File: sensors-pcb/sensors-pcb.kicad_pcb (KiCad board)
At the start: 2 copper layers, 75 x 55 mm, 60 parts, among them J1 Network Connector, J2 STDC14, J3 Conn_Coaxial, SW1 SW_Push, U1 MAX-M8Q, U3 LD39050PU33R, U4 STM32G474RBT6, U5 SN65HVD230, U6 MPU-6050, Y2 8MHz

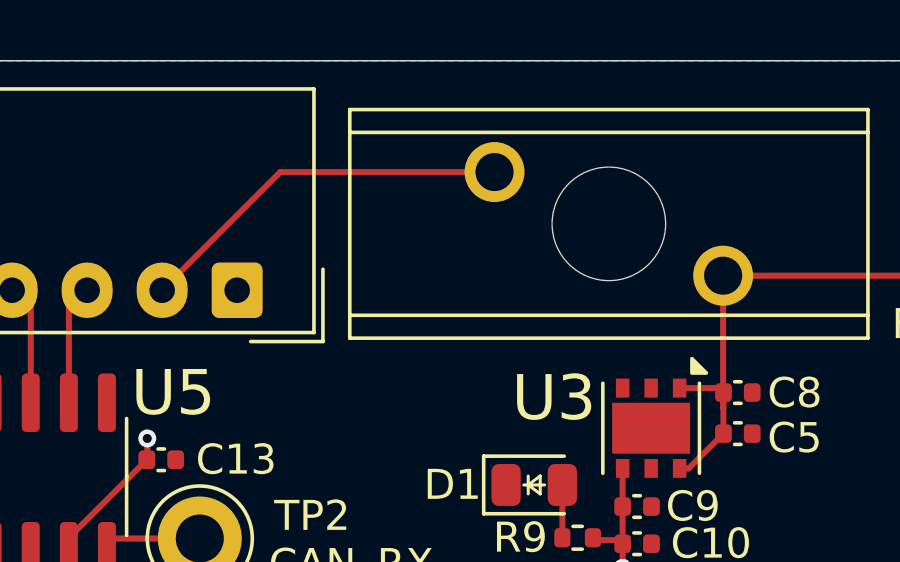
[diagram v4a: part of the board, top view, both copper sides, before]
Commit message: sensors-pcb: add test point for fuse
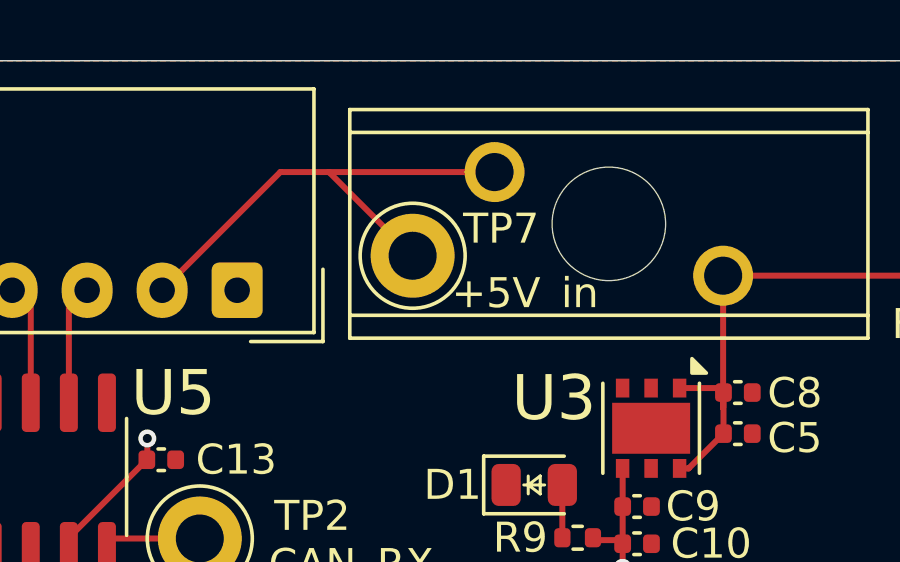
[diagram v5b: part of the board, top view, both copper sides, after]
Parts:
- added TP7: TestPoint, TestPoint:TestPoint_Keystone_5005-5009_Compact, F.Cu at (227.8, 28.0)
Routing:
- net Net-(J1-+5V): track 12.7 -> 16.7 mm
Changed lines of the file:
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@@
 		)
 	)
+	(footprint "TestPoint:TestPoint_Keystone_5005-5009_Compact"
+		(layer "F.Cu")
+		(at 227.85 28)
+		(descr "Keystone THM Compact Test Point 5005-5009, http://www.keyelco.com/product-pdf.cfm?p=1314")
+		(tags "Through Hole Mount Test Points")
+		(property "Reference" "TP7"
+			(at 2.95 -0.9 0)
+			(layer "F.SilkS")
+			(effects
+				(font
+					(size 1 1)
+					(thickness 0.15)
+				)
+			)
+		)
+		(property "Value" "TestPoint"
+			(at 0 3.15 0)
+			(layer "F.Fab")
+			(hide yes)
+			(effects
+				(font
+					(size 1 1)
+					(thickness 0.15)
+				)
+			)
+		)
+		(property "Datasheet" "https://www.keyelco.com/userAssets/file/M65p56.pdf"
+			(at 0 0 0)
+			(unlocked yes)
+			(layer "F.Fab")
+			(hide yes)
+			(effects
+				(font
+					(size 1.27 1.27)
+					(thickness 0.15)
+				)
+			)
+		)
+		(property "Description" "test point"
+			(at 0 0 0)
+			(unlocked yes)
+			(layer "F.Fab")
+			(hide yes)
+			(effects
+				(font
+					(size 1.27 1.27)
+					(thickness 0.15)
+				)
+			)
+		)
+		(property "Net Label" "+5V_in"
+			(at 3.75 1.25 0)
+			(unlocked yes)
+			(layer "F.SilkS")
+			(effects
+				(font
+					(size 1 1)
+					(thickness 0.15)
+				)
+			)
+		)
+		(property ki_fp_filters "Pin* Test*")
+		(sheetname "/STM32 Base Layout/")
+		(sheetfile "stm32_base.kicad_sch")
+		(attr through_hole dnp)
+		(fp_circle
+			(center 0 0)
+			(end 1.75 0)
+			(stroke
+				(width 0.12)
+				(type solid)
+			)
+			(fill no)
+			(layer "F.SilkS")
+		)
+		(fp_circle
+			(center 0 0)
+			(end 2 0)
+			(stroke
+				(width 0.05)
+				(type solid)
+			)
+			(fill no)
+			(layer "F.CrtYd")
+		)
+		(fp_rect
+			(start -1.25 -0.4)
+			(end 1.25 0.4)
+			(stroke
+				(width 0.1)
+				(type default)
+			)
+			(fill no)
+			(layer "F.Fab")
+		)
+		(fp_circle
+			(center 0 0)
+			(end 1.6 0)
+			(stroke
+				(width 0.1)
+				(type solid)
+			)
+			(fill no)
+			(layer "F.Fab")
+		)
+		(fp_text user "${REFERENCE}"
+			(at 0 0 0)
+			(layer "F.Fab")
+			(effects
+				(font
+					(size 0.6 0.6)
+					(thickness 0.09)
+				)
+			)
+		)
+		(pad "1" thru_hole circle
+			(at 0 0)
+			(size 2.8 2.8)
+			(drill 1.6)
+			(layers "*.Cu" "*.Mask")
+			(remove_unused_layers no)
+			(net 9 "Net-(J1-+5V)")
+			(pinfunction "1")
+			(pintype "passive")
+		)
+		(embedded_fonts no)
+		(model "${KICAD9_3DMODEL_DIR}/TestPoint.3dshapes/TestPoint_Keystone_5005-5009_Compact.step"
+			(offset
+				(xyz 0 0 0)
+			)
+			(scale
+				(xyz 1 1 1)
+			)
+			(rotate
+				(xyz 0 0 0)
+			)
+		)
+	)
 	(footprint "Exocet:Fuse_Holder_Littelfuse_01530008"
 		(layer "F.Cu")
@@
 	(segment
 		(start 223.44 25.21)
+		(end 225.06 25.21)
+		(width 0.2)
+		(layer "F.Cu")
+		(net 9)
+	)
+	(segment
+		(start 227.85 28)
+		(end 225.06 25.21)
+		(width 0.2)
+		(layer "F.Cu")
+		(net 9)
+	)
+	(segment
+		(start 225.06 25.21)
 		(end 230.58 25.21)
 		(width 0.2)

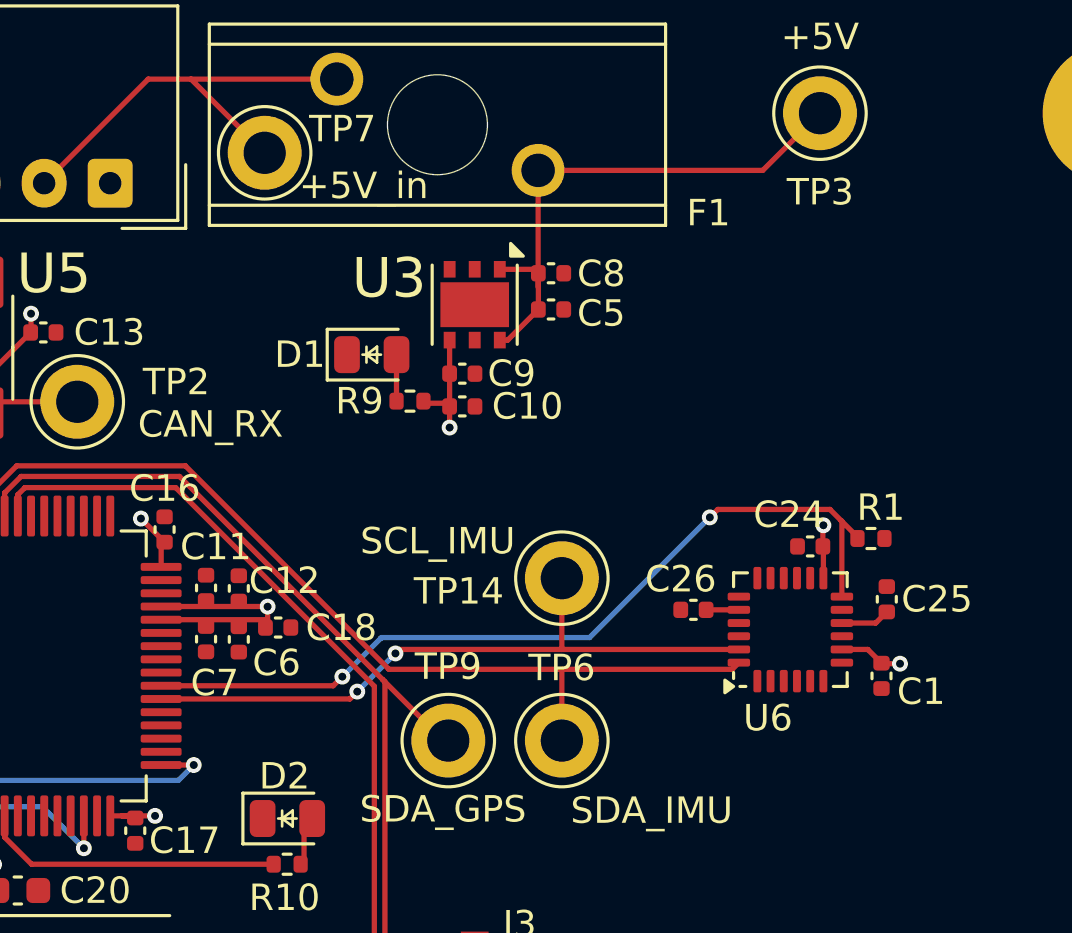
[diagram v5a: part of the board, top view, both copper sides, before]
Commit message: sensors-pcb: add pull-up resistors
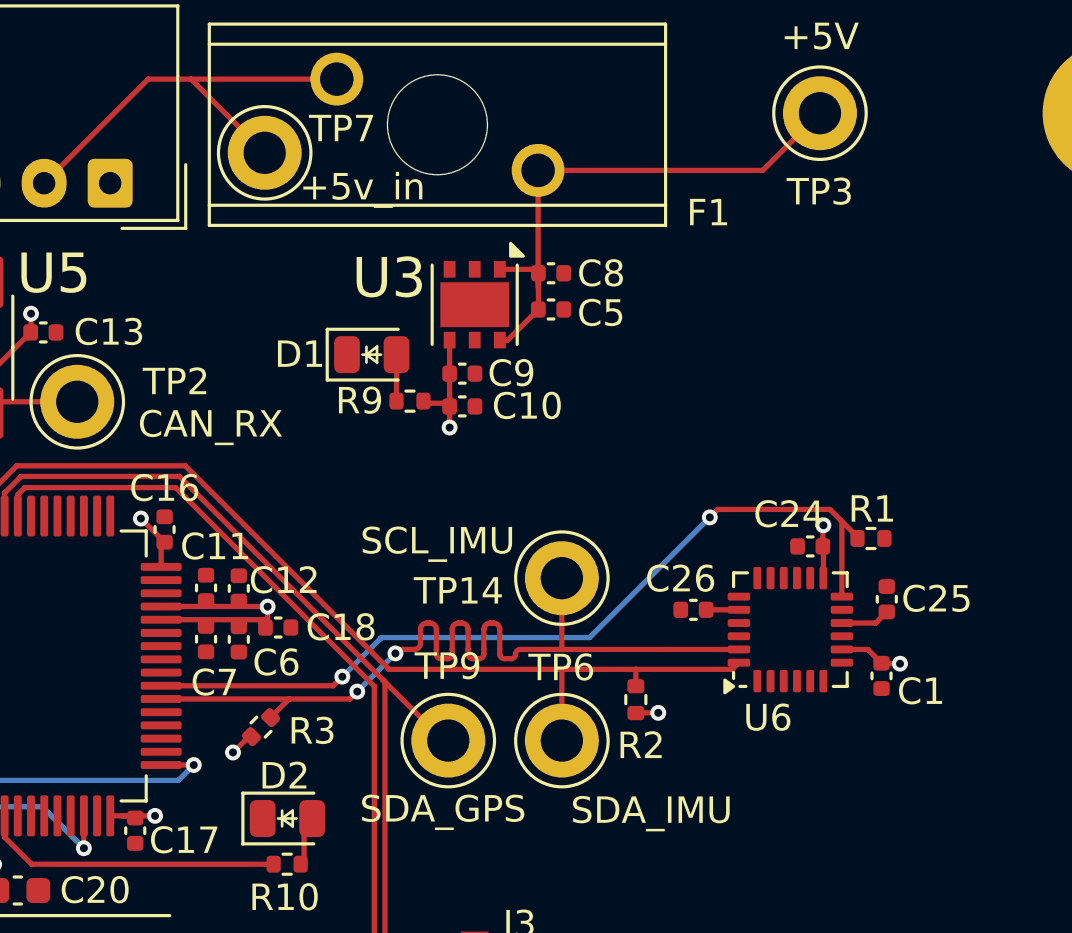
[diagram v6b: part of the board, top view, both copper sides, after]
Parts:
- added R2: 10k, Resistor_SMD:R_0402_1005Metric, F.Cu at (241.9, 48.7)
- added R3: 10k, Resistor_SMD:R_0402_1005Metric, F.Cu at (227.7, 49.7)
- R1: value 100k -> 22k
- turned R1 to 180 degrees
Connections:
- R1 pad 1: /INT_IMU -> +3.3V
- R1 pad 2: GND -> /INT_IMU
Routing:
- net /SCL_IMU: track 25.3 -> 33.1 mm
- net +3.3V: track 39.9 -> 41.7 mm, vias 12 -> 14
- net /SDA_IMU: track 35.6 -> 36.3 mm
